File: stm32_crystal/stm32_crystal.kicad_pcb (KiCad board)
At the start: 2 copper layers, 22 parts, among them U1 STM32F103C6Tx, Y1 Crystal_Small, Y2 8Mhz

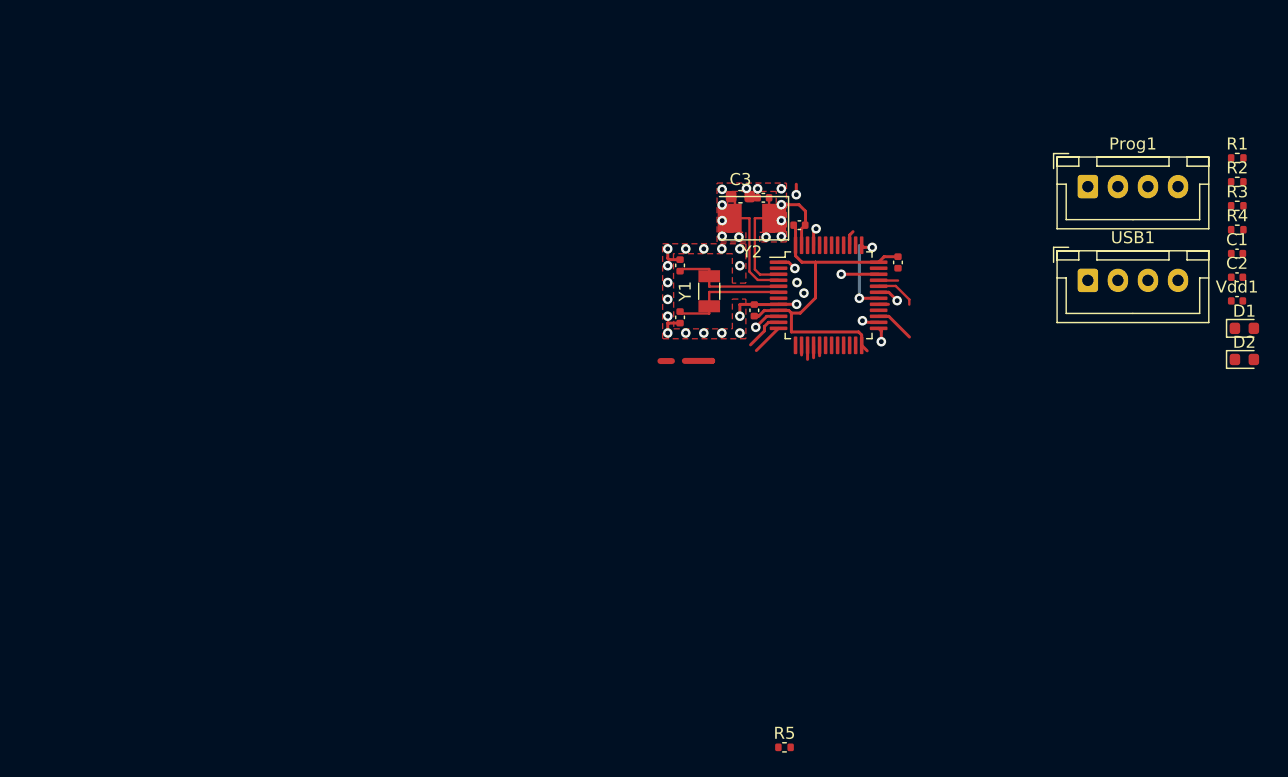
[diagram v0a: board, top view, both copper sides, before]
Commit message: update stm32 cristal
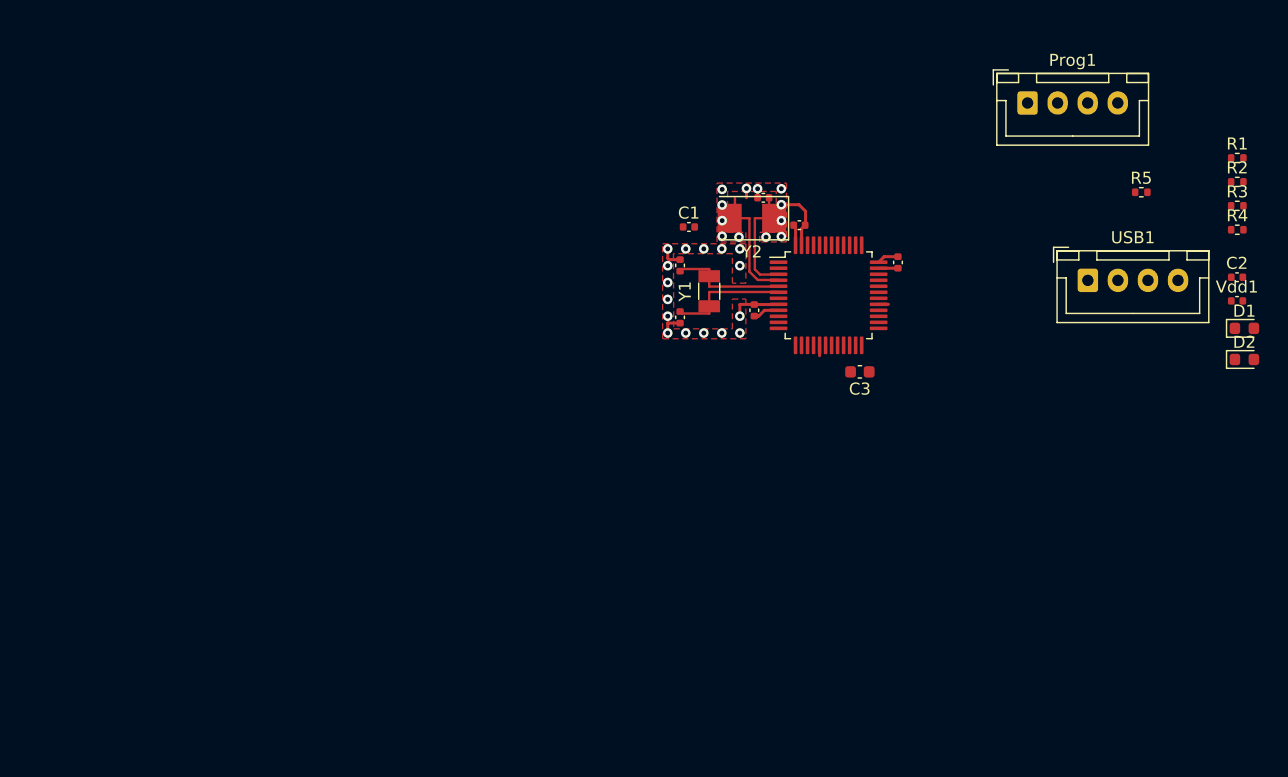
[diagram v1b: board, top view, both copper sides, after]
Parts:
- moved R5 54.9 mm to (210.9, 89.5)
- moved C1 45.6 mm to (173.3, 92.4)
- moved C3 17.6 mm to (187.5, 104.5), turned to 180 degrees
- moved Prog1 8.57 mm to (201.5, 82.1)
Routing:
- net +3V3: track 29.5 -> 5.75 mm
- net unconnected-(U1-PA9-Pad30): track 6.00 -> 0.00 mm, vias 1 -> 0
- net /D-: track 3.45 -> 0.00 mm
- net unconnected-(U1-PA1-Pad11): track 3.33 -> 0.00 mm
- net unconnected-(U1-PB14-Pad27): track 3.28 -> 0.00 mm
- net Swdio: track 3.11 -> 0.00 mm, vias 1 -> 0
- net unconnected-(U1-PA2-Pad12): track 2.62 -> 0.00 mm
- net unconnected-(U1-PA0-Pad10): track 2.27 -> 0.00 mm, vias 1 -> 0
- net GND: track 18.7 -> 16.5 mm, vias 31 -> 28
- net (no net): track 1.83 -> 0.00 mm, vias 1 -> 0
- net unconnected-(U1-PA10-Pad31): track 1.83 -> 0.00 mm, vias 1 -> 0
- net /D+: track 1.62 -> 0.04 mm
- net V_Bat: track 1.57 -> 0.00 mm, vias 1 -> 0
- net unconnected-(U1-PB8-Pad45): track 1.46 -> 0.00 mm, vias 1 -> 0
- net unconnected-(U1-PB13-Pad26): track 1.40 -> 0.00 mm, vias 1 -> 0
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
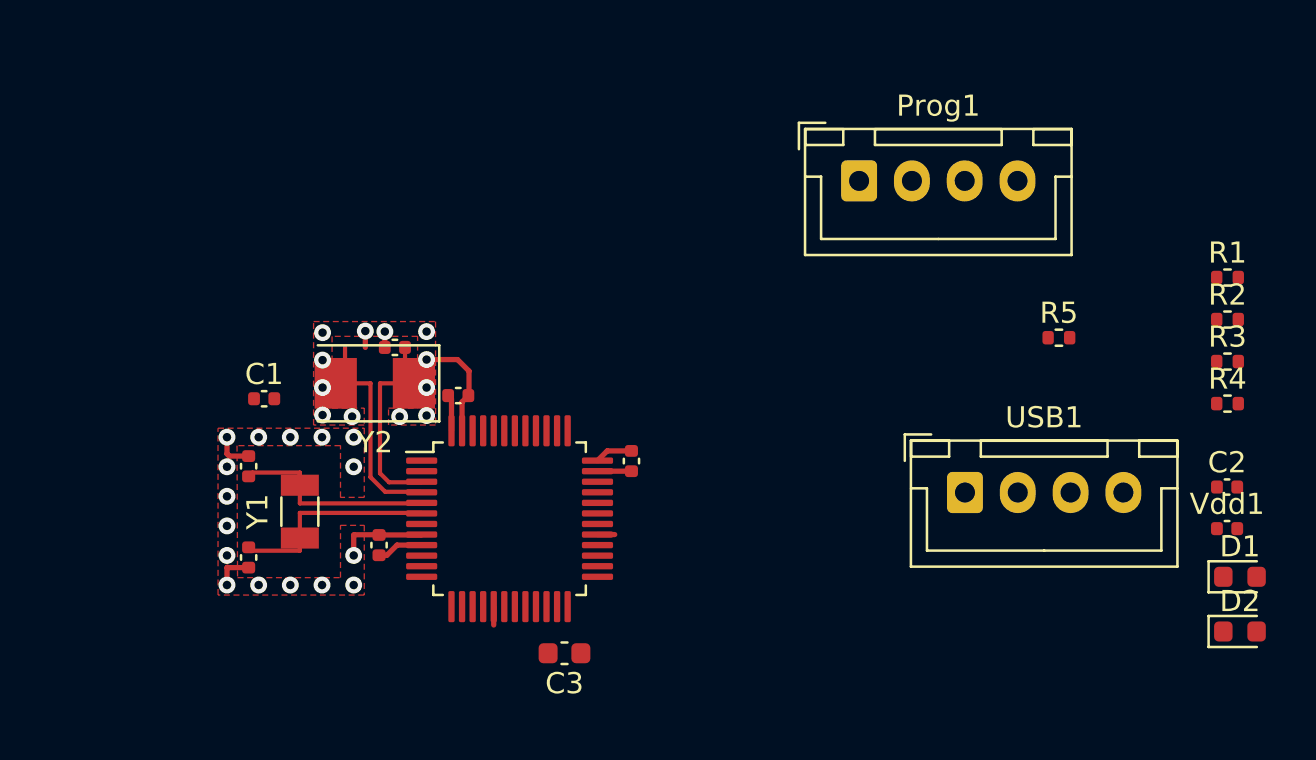
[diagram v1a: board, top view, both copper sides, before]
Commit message: changes in stm and add can module
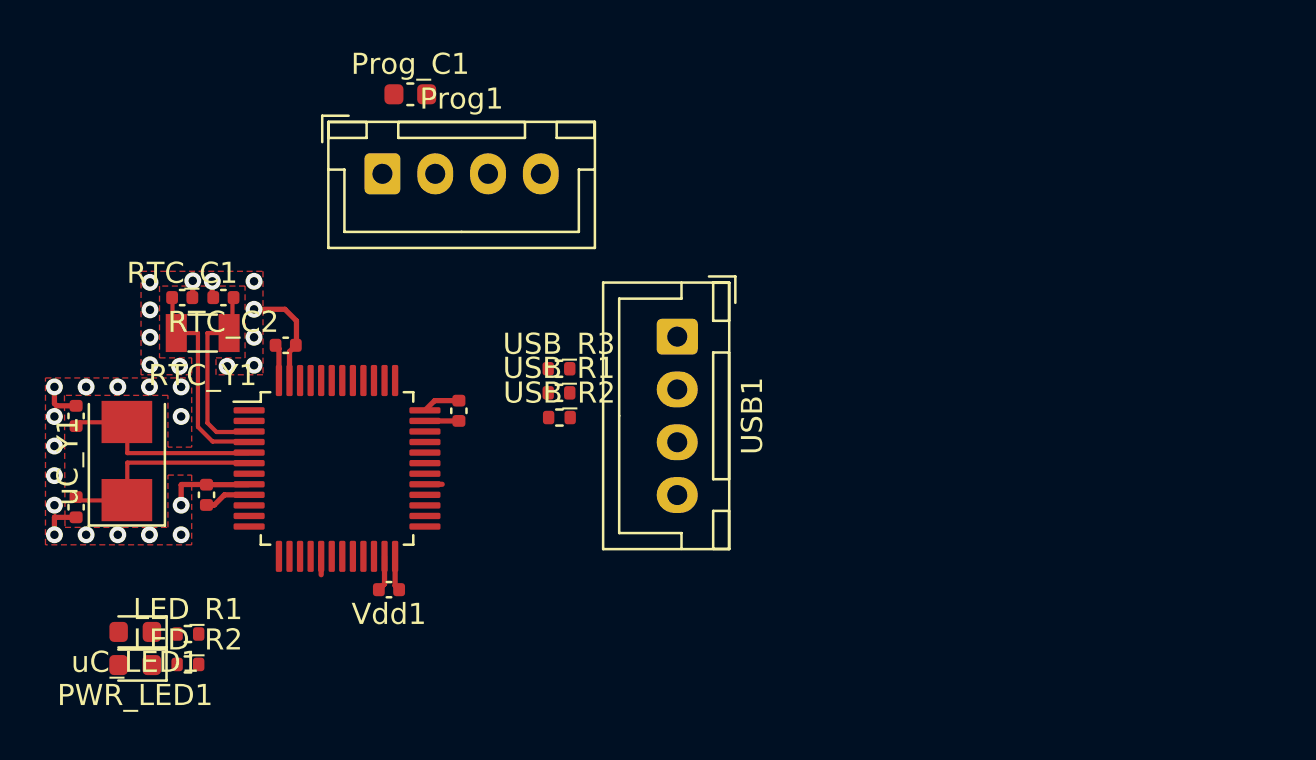
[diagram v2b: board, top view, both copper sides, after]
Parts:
- removed C1, C2, C4: 22pF, Capacitor_SMD:C_0402_1005Metric
- removed C3: 104, Capacitor_SMD:C_0603_1608Metric
- removed D1, D2: LED, LED_SMD:LED_0603_1608Metric
- removed R1, R2: 510, Resistor_SMD:R_0402_1005Metric
- removed R3: 4.7k, Resistor_SMD:R_0402_1005Metric
- removed R4, R5: 20, Resistor_SMD:R_0402_1005Metric
- removed Y1: Crystal_Small, Crystal:Crystal_SMD_3215-2Pin_3.2x1.5mm
- removed Y2: 8Mhz, Crystal:Crystal_SMD_5032-2Pin_5.0x3.2mm
- added LED_R1: 510, Resistor_SMD:R_0402_1005Metric, F.Cu at (169.7, 103.5)
- added LED_R2: 510, Resistor_SMD:R_0402_1005Metric, F.Cu at (169.7, 105.0)
- added PWR_LED1: LED, LED_SMD:LED_0603_1608Metric, F.Cu at (167.2, 105.0)
- added Prog_C1: 104, Capacitor_SMD:C_0603_1608Metric, F.Cu at (180.2, 78.0)
- added RTC_C1: 22pF, Capacitor_SMD:C_0402_1005Metric, F.Cu at (169.4, 87.6)
- added RTC_C2: 22pF, Capacitor_SMD:C_0402_1005Metric, F.Cu at (171.4, 87.6)
- added RTC_Y1: Crystal_Small, Crystal:Crystal_SMD_3215-2Pin_3.2x1.5mm, F.Cu at (170.4, 89.3)
- added USB_R1: 20, Resistor_SMD:R_0402_1005Metric, F.Cu at (187.2, 92.1)
- added USB_R2: 20, Resistor_SMD:R_0402_1005Metric, F.Cu at (187.3, 93.3)
- added USB_R3: 4.7k, Resistor_SMD:R_0402_1005Metric, F.Cu at (187.2, 91.0)
- added uC_LED1: LED, LED_SMD:LED_0603_1608Metric, F.Cu at (167.2, 103.4)
- added uC_Y1: 8Mhz, Crystal:Crystal_SMD_5032-2Pin_5.0x3.2mm, F.Cu at (166.8, 95.3)
- moved Vdd1 39.8 mm to (179.2, 101.4), turned to 180 degrees
- moved Prog1 22.6 mm to (178.9, 81.8)
- moved USB1 15.5 mm to (192.8, 89.5), turned to -90 degrees
- moved CC2 8.51 mm to (164.4, 97.5)
- moved CC1 8.51 mm to (164.4, 93.2)
- moved Vdd3 8.51 mm to (182.5, 93.0)
- moved U1 8.51 mm to (176.7, 95.7)
- moved Vdd2 8.51 mm to (170.6, 97.0)
- moved Vdd4 8.51 mm to (174.3, 89.9)
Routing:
- net GND: track 16.5 -> 18.2 mm
- net +3V3: track 5.75 -> 7.40 mm

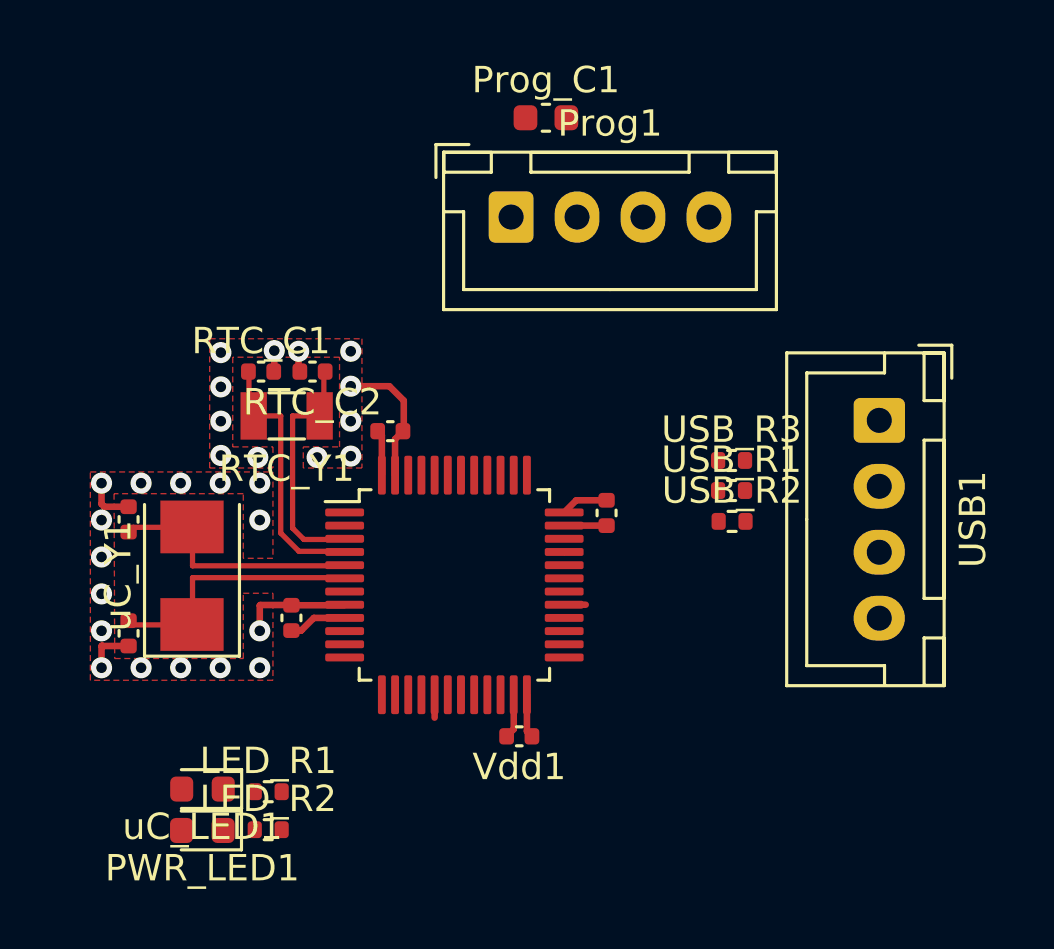
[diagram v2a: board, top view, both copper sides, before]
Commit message: changes power_supply_buck_5v add layout
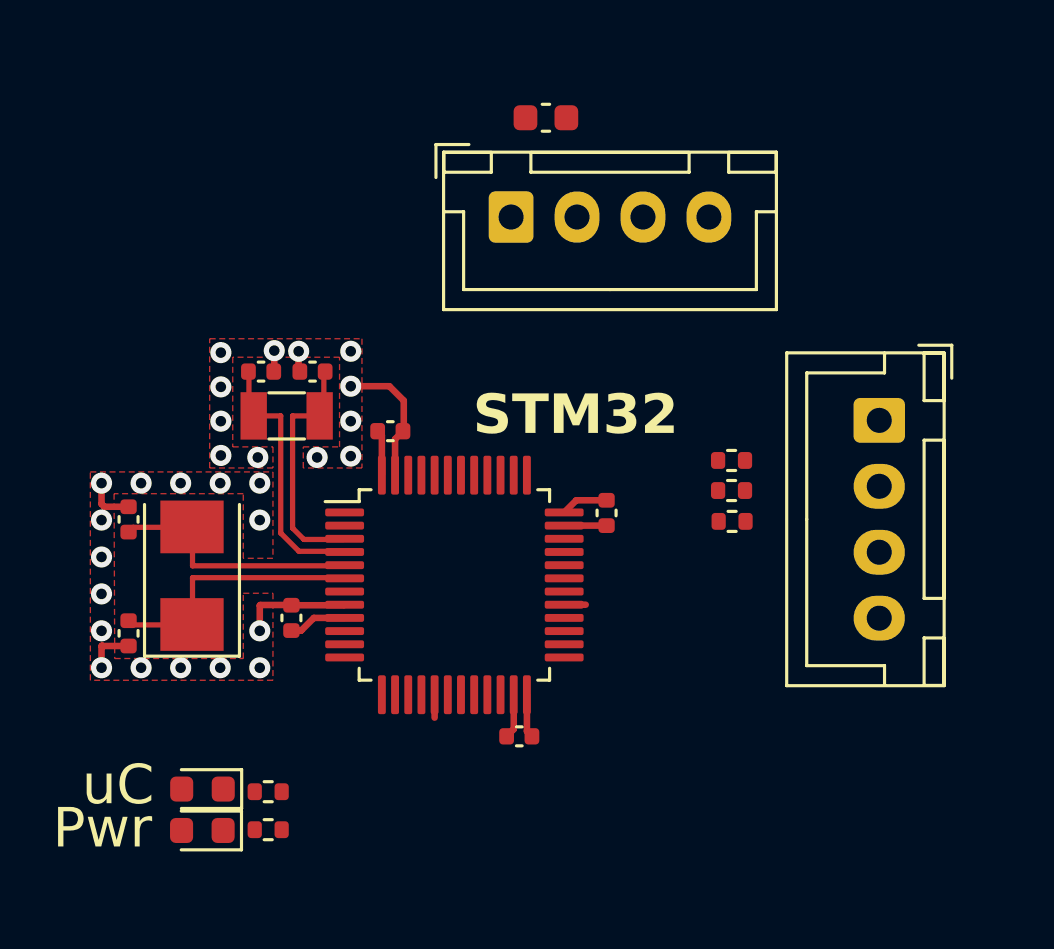
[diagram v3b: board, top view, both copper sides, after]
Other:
- board text added: "Pwr"
- board text added: "STM32"
- board text added: "uC"
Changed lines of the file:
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@@
     (property "ki_keywords" "R res resistor")
     (attr smd)
-    (fp_text reference "USB_R1" (at 0 -1.17) (layer "F.SilkS")
+    (fp_text reference "USB_R1" (at 0 -1.17) (layer "F.SilkS") hide
         (effects (font (size 1 1) (thickness 0.15)))
     )
@@
     (property "ki_keywords" "cap capacitor")
     (attr smd)
-    (fp_text reference "Prog_C1" (at 0 -1.43) (layer "F.SilkS")
+    (fp_text reference "Prog_C1" (at 0 -1.43) (layer "F.SilkS") hide
         (effects (font (size 1 1) (thickness 0.15)))
     )
@@
     (property "ki_keywords" "connector")
     (attr through_hole)
-    (fp_text reference "USB1" (at 3.75 -3.55 90) (layer "F.SilkS")
+    (fp_text reference "USB1" (at 3.75 -3.55 90) (layer "F.SilkS") hide
         (effects (font (size 1 1) (thickness 0.15)))
     )
@@
     (property "ki_keywords" "cap capacitor")
     (attr smd)
-    (fp_text reference "RTC_C2" (at 0 -1.16) (layer "F.SilkS")
+    (fp_text reference "RTC_C2" (at 0 -1.16) (layer "F.SilkS") hide
         (effects (font (size 1 1) (thickness 0.15)))
     )
@@
     (property "ki_keywords" "R res resistor")
     (attr smd)
-    (fp_text reference "USB_R3" (at 0 -1.17) (layer "F.SilkS")
+    (fp_text reference "USB_R3" (at 0 -1.17) (layer "F.SilkS") hide
         (effects (font (size 1 1) (thickness 0.15)))
     )
@@
     (property "ki_keywords" "quartz ceramic resonator oscillator")
     (attr smd)
-    (fp_text reference "uC_Y1" (at 0 -2.8 90) (layer "F.SilkS")
+    (fp_text reference "uC_Y1" (at 0 -2.8 90) (layer "F.SilkS") hide
         (effects (font (size 1 1) (thickness 0.15)))
     )
@@
     (property "ki_keywords" "R res resistor")
     (attr smd)
-    (fp_text reference "LED_R1" (at 0 -1.17) (layer "F.SilkS")
+    (fp_text reference "LED_R1" (at 0 -1.17) (layer "F.SilkS") hide
         (effects (font (size 1 1) (thickness 0.15)))
     )
@@
     (property "ki_keywords" "LED diode")
     (attr smd)
-    (fp_text reference "uC_LED1" (at 0 -1.43) (layer "F.SilkS")
+    (fp_text reference "uC_LED1" (at 0 -1.43) (layer "F.SilkS") hide
         (effects (font (size 1 1) (thickness 0.15)))
     )
@@
     (property "ki_keywords" "connector")
     (attr through_hole)
-    (fp_text reference "Prog1" (at 3.75 -3.55) (layer "F.SilkS")
+    (fp_text reference "Prog1" (at 3.75 -3.55) (layer "F.SilkS") hide
         (effects (font (size 1 1) (thickness 0.15)))
     )
@@
     (property "ki_keywords" "cap capacitor")
     (attr smd)
-    (fp_text reference "Vdd1" (at 0 -1.16) (layer "F.SilkS")
+    (fp_text reference "Vdd1" (at 0 -1.16) (layer "F.SilkS") hide
         (effects (font (size 1 1) (thickness 0.15)))
     )
@@
     (property "ki_keywords" "quartz ceramic resonator oscillator")
     (attr smd)
-    (fp_text reference "RTC_Y1" (at 0 -2) (layer "F.SilkS")
+    (fp_text reference "RTC_Y1" (at 0 -2) (layer "F.SilkS") hide
         (effects (font (size 1 1) (thickness 0.15)))
     )
@@
     (property "ki_keywords" "R res resistor")
     (attr smd)
-    (fp_text reference "USB_R2" (at 0 -1.17) (layer "F.SilkS")
+    (fp_text reference "USB_R2" (at 0 -1.17) (layer "F.SilkS") hide
         (effects (font (size 1 1) (thickness 0.15)))
     )
@@
     (property "ki_keywords" "cap capacitor")
     (attr smd)
-    (fp_text reference "RTC_C1" (at 0 -1.16) (layer "F.SilkS")
+    (fp_text reference "RTC_C1" (at 0 -1.16) (layer "F.SilkS") hide
         (effects (font (size 1 1) (thickness 0.15)))
     )
@@
     (property "ki_keywords" "LED diode")
     (attr smd)
-    (fp_text reference "PWR_LED1" (at 0 -1.43) (layer "F.SilkS")
+    (fp_text reference "PWR_LED1" (at 0 -1.43) (layer "F.SilkS") hide
         (effects (font (size 1 1) (thickness 0.15)))
     )
@@
     (property "ki_keywords" "R res resistor")
     (attr smd)
-    (fp_text reference "LED_R2" (at 0 -1.17) (layer "F.SilkS")
+    (fp_text reference "LED_R2" (at 0 -1.17) (layer "F.SilkS") hide
         (effects (font (size 1 1) (thickness 0.15)))
     )
@@
     )
   )
+  (gr_text "STM32" (at 177.44 90.12) (layer "F.SilkS")
+    (effects (font (size 1.5 1.5) (thickness 0.3) bold) (justify left bottom))
+  )
+  (gr_text "uC" (at 162.62 104.16) (layer "F.SilkS")
+    (effects (font (size 1.5 1.5) (thickness 0.1875)) (justify left bottom))
+  )
+  (gr_text "Pwr" (at 161.51 105.8) (layer "F.SilkS")
+    (effects (font (size 1.5 1.5) (thickness 0.1875)) (justify left bottom))
+  )
   (segment (start 170.155 93.7332) (end 170.155 89.29) (width 0.2) (layer "F.Cu") (net 1))
